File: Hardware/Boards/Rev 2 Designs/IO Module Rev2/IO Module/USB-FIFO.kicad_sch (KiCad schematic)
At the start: 25 parts, among them U13 FT600Q, Y2 30Mhz

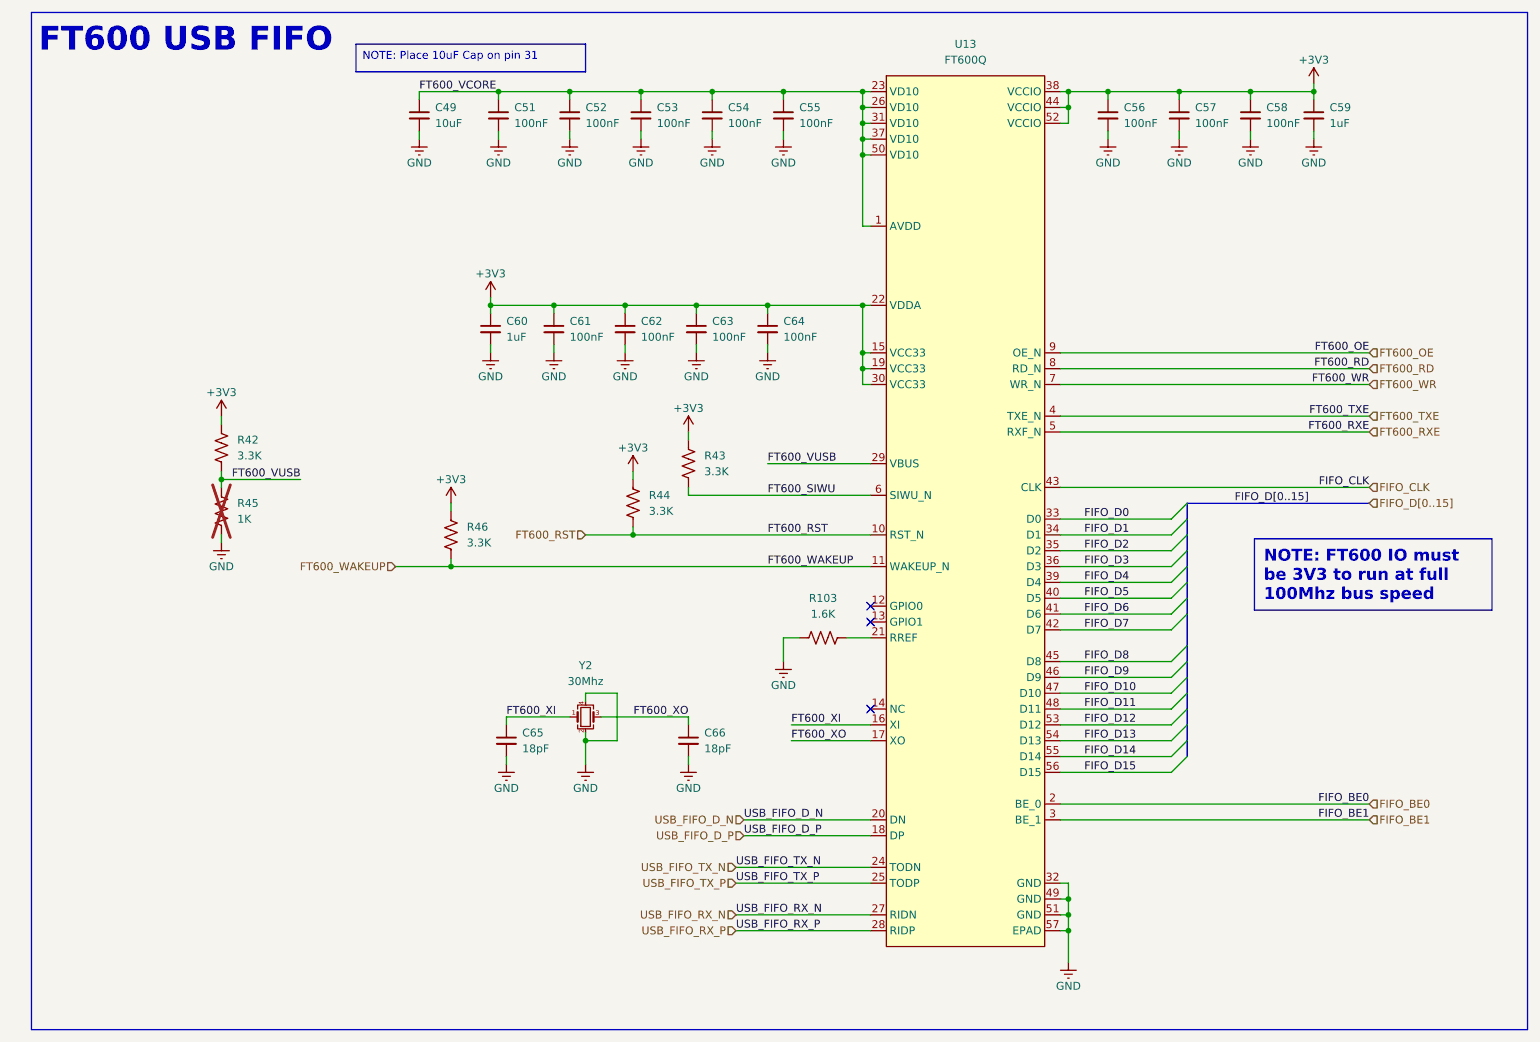
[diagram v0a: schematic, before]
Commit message: Rev 2 IO module complete
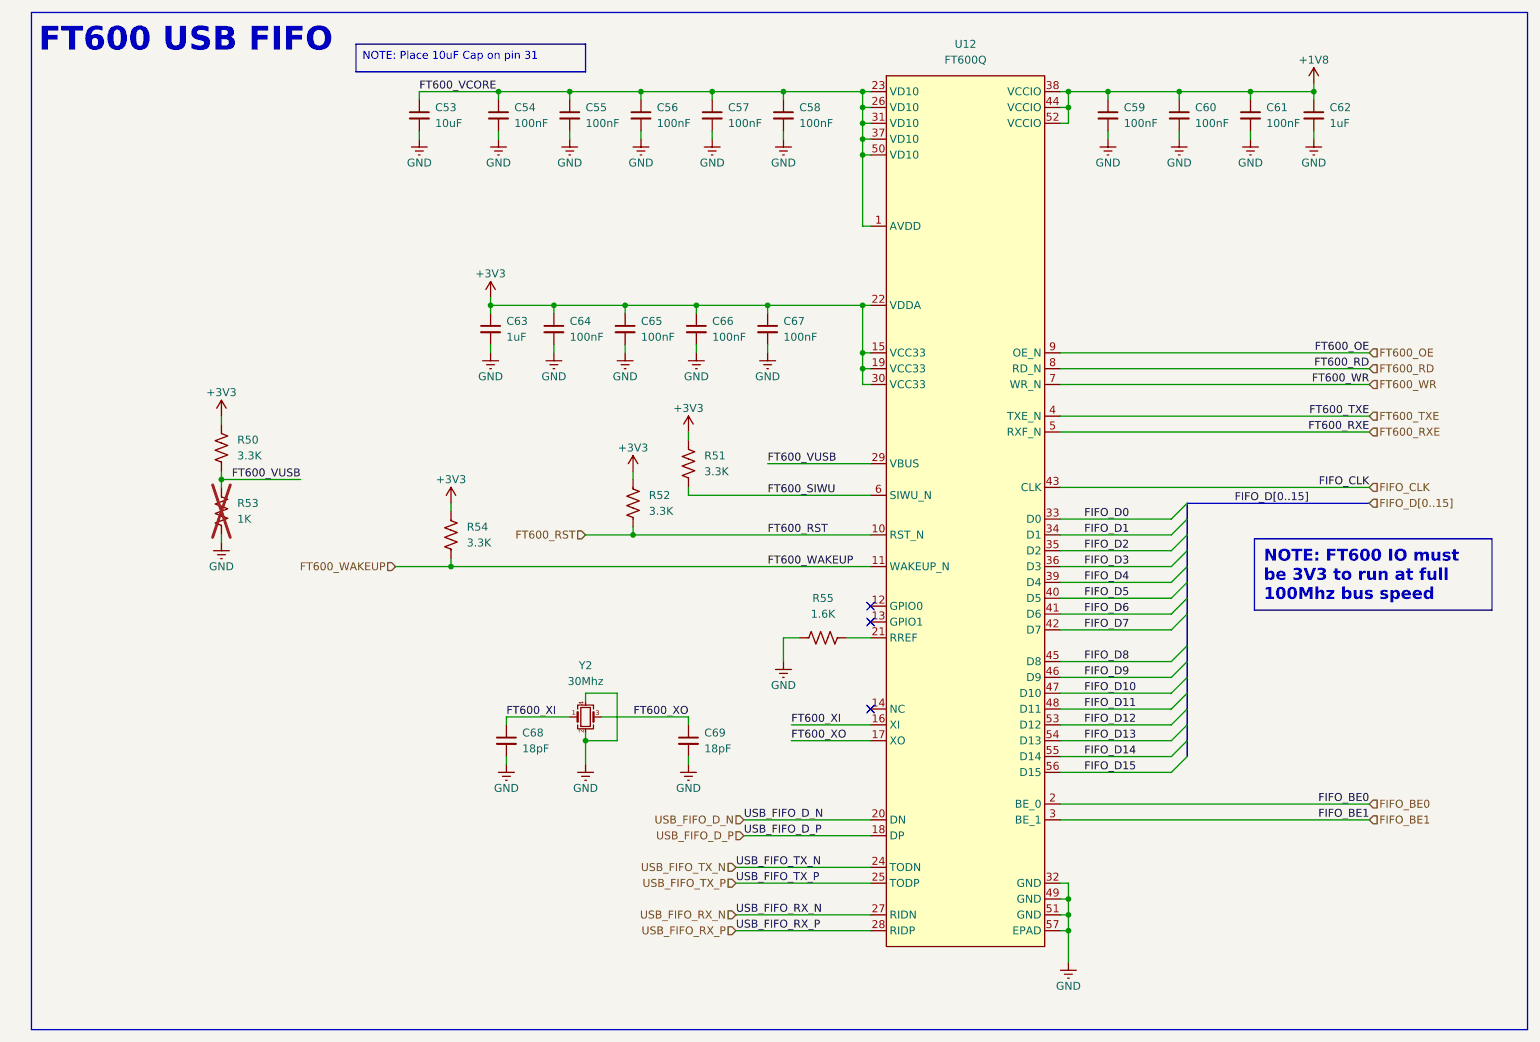
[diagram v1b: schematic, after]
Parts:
- renumbered C49 to C53, C51 to C54, C52 to C55, C53 to C56, C54 to C57, C55 to C58, C56 to C59, C57 to C60, C58 to C61, C59 to C62, C60 to C63, C61 to C64, C62 to C65, C63 to C66, C64 to C67, C65 to C68, C66 to C69, R42 to R50, R43 to R51, R44 to R52, R45 to R53, R46 to R54, R103 to R55, U13 to U12
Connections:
- net +3V3: no longer C59.1, C60.1, C61.1, C62.1, U12.38 (VCCIO), U12.44 (VCCIO), U12.52 (VCCIO)
- new net +1V8: C59.1, C60.1, C61.1, C62.1, U12.38 (VCCIO), U12.44 (VCCIO), U12.52 (VCCIO)
